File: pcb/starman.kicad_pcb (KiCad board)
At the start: 2 copper layers, 35.6 x 68.6 mm, 25 parts, among them J1 Barrel_Jack_MountingPin, J2 Conn_02x09_Odd_Even, J3 Conn_02x09_Odd_Even, J4 Conn_02x03_Odd_Even, J5 Conn_01x06, SW1 SW_SPST, SW2 SW_Push, U1 LF50_TO220, U2 LF33_TO220

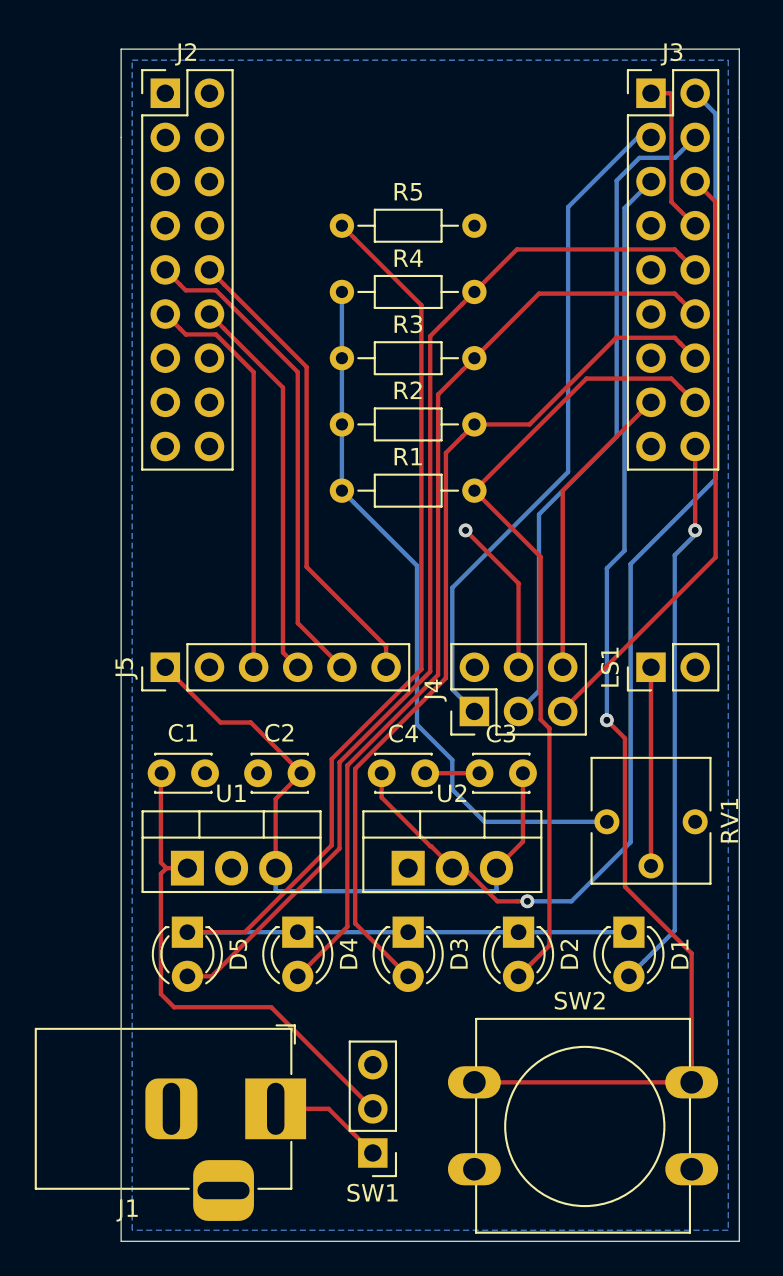
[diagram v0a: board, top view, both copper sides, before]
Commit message: Corrected resistor sizes, capacitor location, programming header.
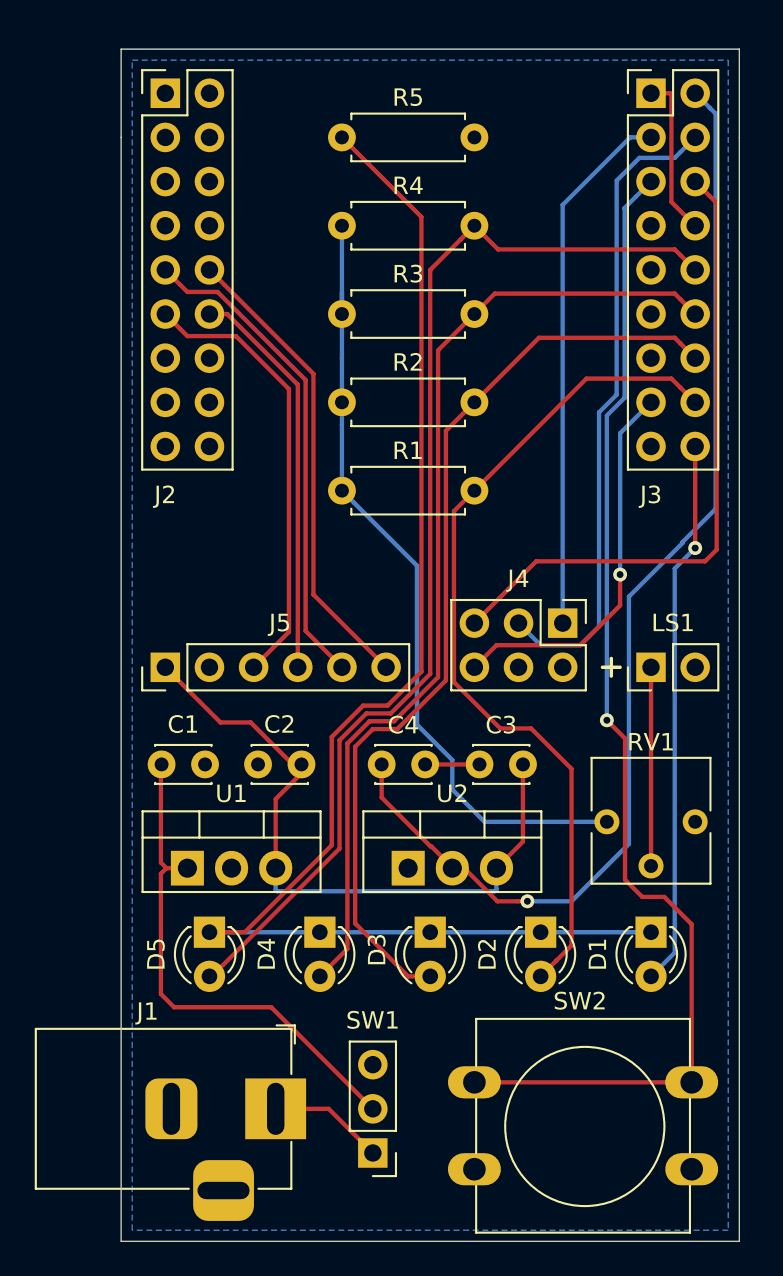
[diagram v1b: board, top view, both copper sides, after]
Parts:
- R1, R2, R3, R4, R5: footprint Resistor_THT:R_Axial_DIN0204_L3.6mm_D1.6mm_P7.62mm_Horizontal -> Resistor_THT:R_Axial_DIN0207_L6.3mm_D2.5mm_P7.62mm_Horizontal
- moved J4 7.18 mm to (127.0, 109.2), turned to 270 degrees
- moved R5 5.08 mm to (114.3, 81.3)
- moved R4 3.81 mm to (121.9, 86.4)
- moved R3 2.54 mm to (114.3, 91.4)
- moved D1 1.27 mm to (132.1, 127.0)
- moved D2 1.27 mm to (125.7, 127.0)
- moved D5 1.27 mm to (106.7, 127.0)
- moved R2 1.27 mm to (114.3, 96.5)
- moved D3 1.27 mm to (119.4, 127.0)
- moved D4 1.27 mm to (113.0, 127.0)
- moved C1 0.51 mm to (106.4, 117.3)
- moved C2 0.51 mm to (112.0, 117.3)
- moved C3 0.51 mm to (122.2, 117.3)
- moved C4 0.51 mm to (116.6, 117.3)
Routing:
- net GND: track 21.6 -> 12.4 mm, vias 1 -> 0
- net /EN: track 38.7 -> 31.5 mm
- net Net-(R1-Pad1): track 40.9 -> 46.0 mm
- net /BOOT: track 17.3 -> 22.3 mm, vias 0 -> 1
- net Net-(D1-Pad1): track 75.4 -> 80.1 mm
- net /CHAN2: track 51.1 -> 53.9 mm
- net /CHAN4: track 61.2 -> 64.0 mm
- net /RXD: track 34.6 -> 37.4 mm
- net /CHAN1: track 46.4 -> 48.9 mm
- net /DATA: track 23.4 -> 25.7 mm
- net /CHAN3: track 54.5 -> 56.3 mm
- net /TXD: track 38.4 -> 37.2 mm
- net /BUTTON: track 67.4 -> 68.1 mm
- net /CLOCK: track 22.4 -> 23.0 mm
- net /STATUS: track 32.1 -> 31.5 mm

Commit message: Minor adjustments to resistors and some placements
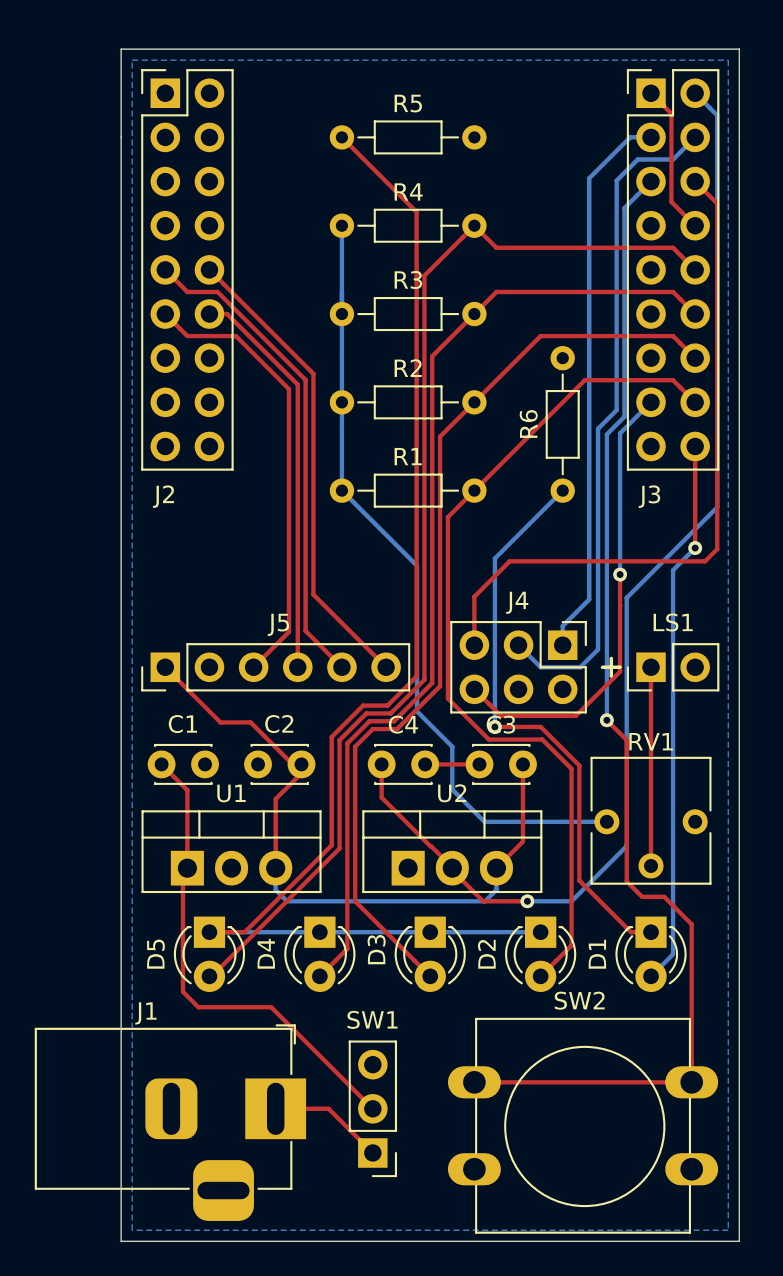
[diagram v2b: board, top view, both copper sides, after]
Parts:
- added R6: 330, Resistor_THT:R_Axial_DIN0204_L3.6mm_D1.6mm_P7.62mm_Horizontal, F.Cu at (127.0, 101.6)
- R1, R2, R3, R4: value 50 -> 75; footprint Resistor_THT:R_Axial_DIN0207_L6.3mm_D2.5mm_P7.62mm_Horizontal -> Resistor_THT:R_Axial_DIN0204_L3.6mm_D1.6mm_P7.62mm_Horizontal
- R5: footprint Resistor_THT:R_Axial_DIN0207_L6.3mm_D2.5mm_P7.62mm_Horizontal -> Resistor_THT:R_Axial_DIN0204_L3.6mm_D1.6mm_P7.62mm_Horizontal
- moved J4 1.27 mm to (127.0, 110.5)
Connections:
- D2 pad 1: Net-(D1-Pad1) -> Net-(D2-Pad1)
- D3 pad 1: Net-(D1-Pad1) -> Net-(D2-Pad1)
- D4 pad 1: Net-(D1-Pad1) -> Net-(D2-Pad1)
- D5 pad 1: Net-(D1-Pad1) -> Net-(D2-Pad1)
- R5 pad 1: Net-(D1-Pad1) -> Net-(D2-Pad1)
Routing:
- net Net-(D2-Pad1): track 0.00 -> 73.5 mm
- net Net-(D1-Pad1): track 80.1 -> 33.0 mm, vias 0 -> 1
- net /BOOT: track 22.3 -> 26.3 mm
- net /RXD: track 37.4 -> 39.6 mm
- net /EN: track 31.5 -> 33.0 mm
- net Net-(C1-Pad2): track 29.1 -> 27.7 mm
- net /TXD: track 37.2 -> 38.5 mm
- net /CHAN1: track 48.9 -> 49.9 mm
- net /CHAN2: track 53.9 -> 53.3 mm
- net GND: track 12.4 -> 11.8 mm
